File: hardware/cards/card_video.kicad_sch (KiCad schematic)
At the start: 48 parts, among them J1 HDMI_A, J2 VGA HD15, M1 Core2350B (8MB PSRAM), U2 74LVC245A, U3 74LVC245A, U4 74LVC245A, U5 74LVC245A, U6 74LVC245A, U7 74LVC245A

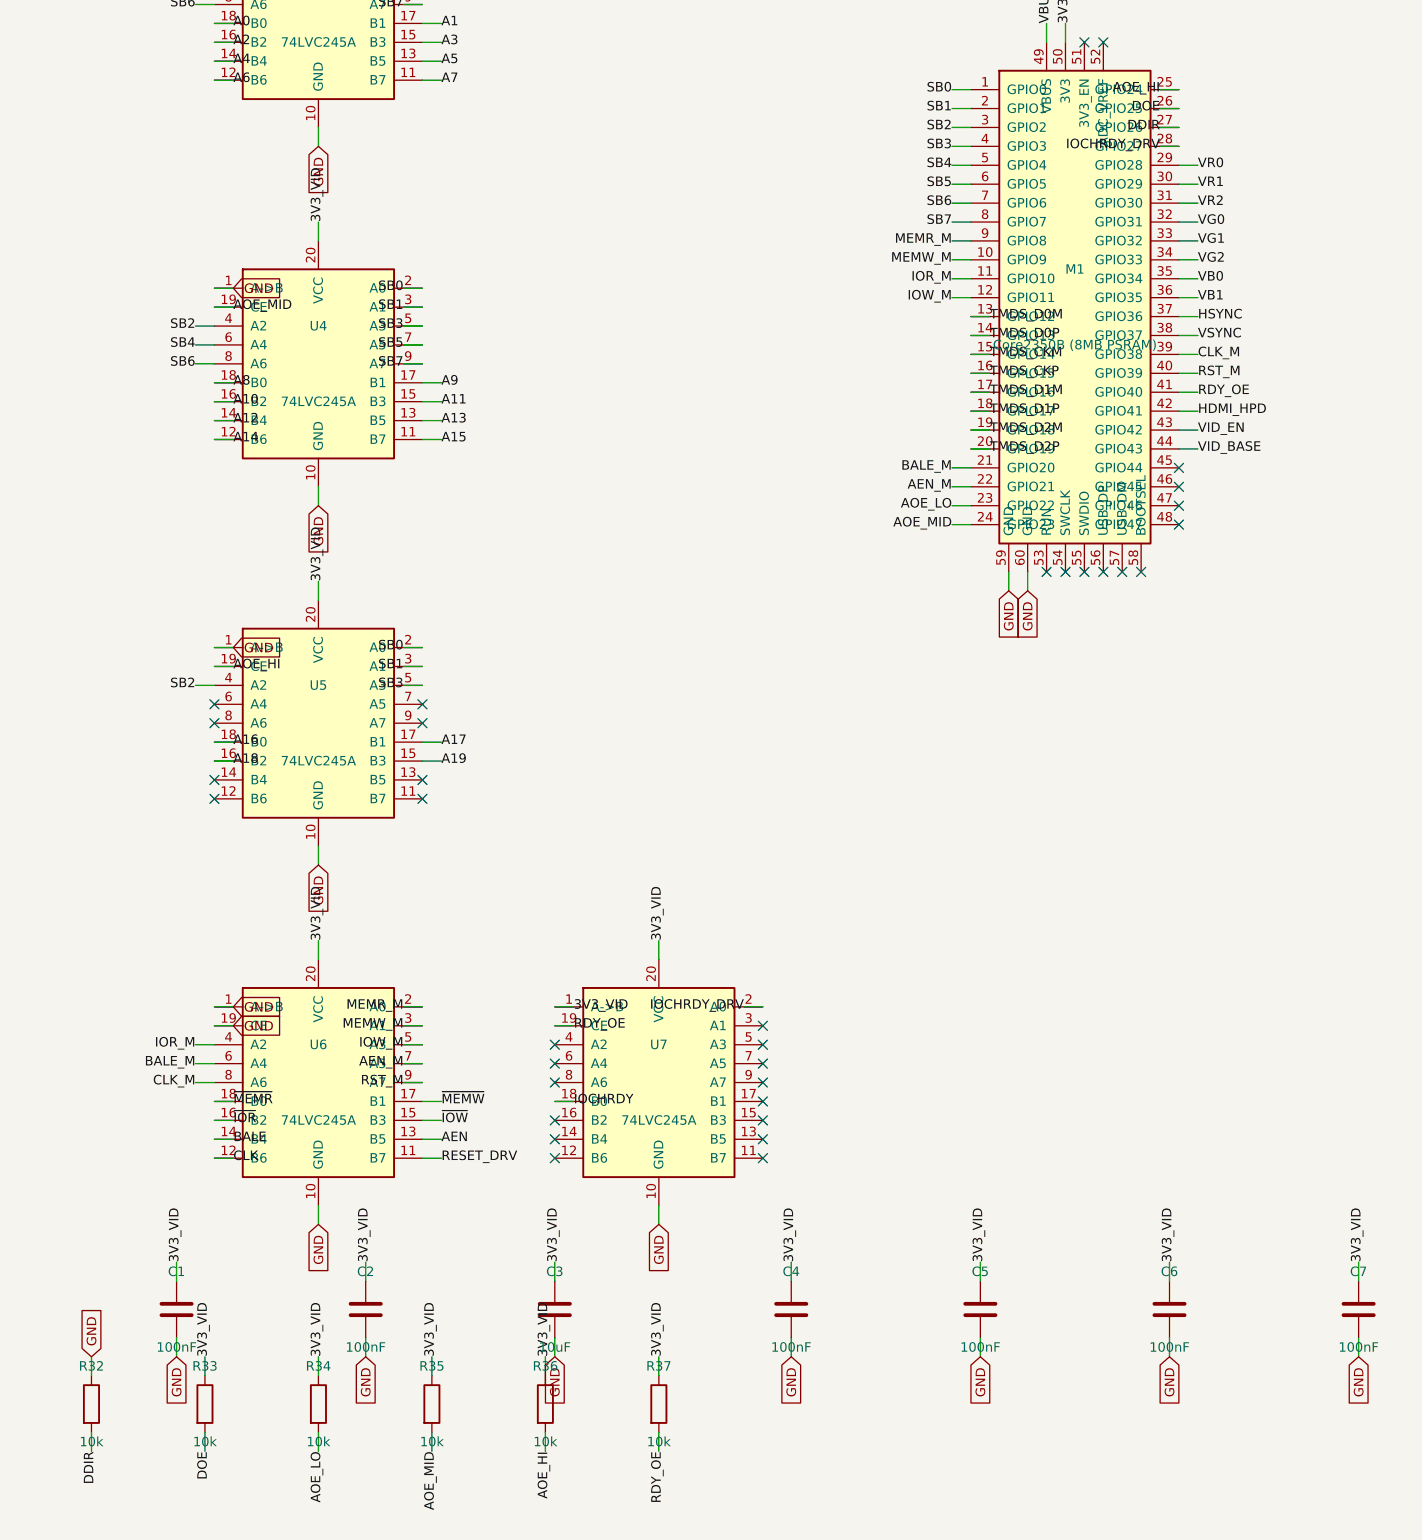
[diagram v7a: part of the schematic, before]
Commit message: sidecar: isolation/buffer bank -- 5V-compatible ISA expansion port
Rewrite the sidecar from a passive 60-pin pass-through into the 3.3V board's
only real-ISA attachment point: an LVC buffer bank (5V-tolerant inputs,
3.3V-TTL outputs) between the internal bus and an external ISA header whose
bus-side nets are port-local (X_*, via isa_conn remap).

- Outbound: 3x 74LVC245A (A0-19 + BALE/AEN/CLK/OSC, DIR strapped outbound) +
  2x 74LVC244A (MEMR/MEMW/IOR/IOW, RESET_DRV, TC, DACK1-3, REFRESH).
- Data: 1x 74LVC245A, DIR = EXP_DDIR, R1 pulls it outbound-safe at power-on
  (DIR=H => A->B; truth table in comment). ~OE tied enabled.
- Inbound: X_IRQ2-7/X_DRQ1-3 -> EXT_* via 2x 74LVC244A, 100k pull-downs on
  every X_ input (unplugged reads all-zeros).
- IOCHRDY/~{IOCHCK}: 74LVC2G07 open-drain (2G06 body + value override) drives
  the internal nets, 10k pull-ups on the X_ side (wired-AND, no contention).
- PINS: filtered copy of isa_conn.ISA_PINS (IRQ/DRQ dropped -> EXT_*), plus
  PRIV_EXP (EXP_DDIR in, EXT_* out); IOCHRDY/~{IOCHCK} kept.

Also refreshes stale build outputs from earlier 3v3 tasks that had edited
sources without rebuilding (network/picogus sheets, card_video net renames),
so committed outputs match current sources. validate_sheet sidecar: zero
structural; build.py exit 0.

Co-Authored-By: Claude Fable 5 <noreply@anthropic.com>
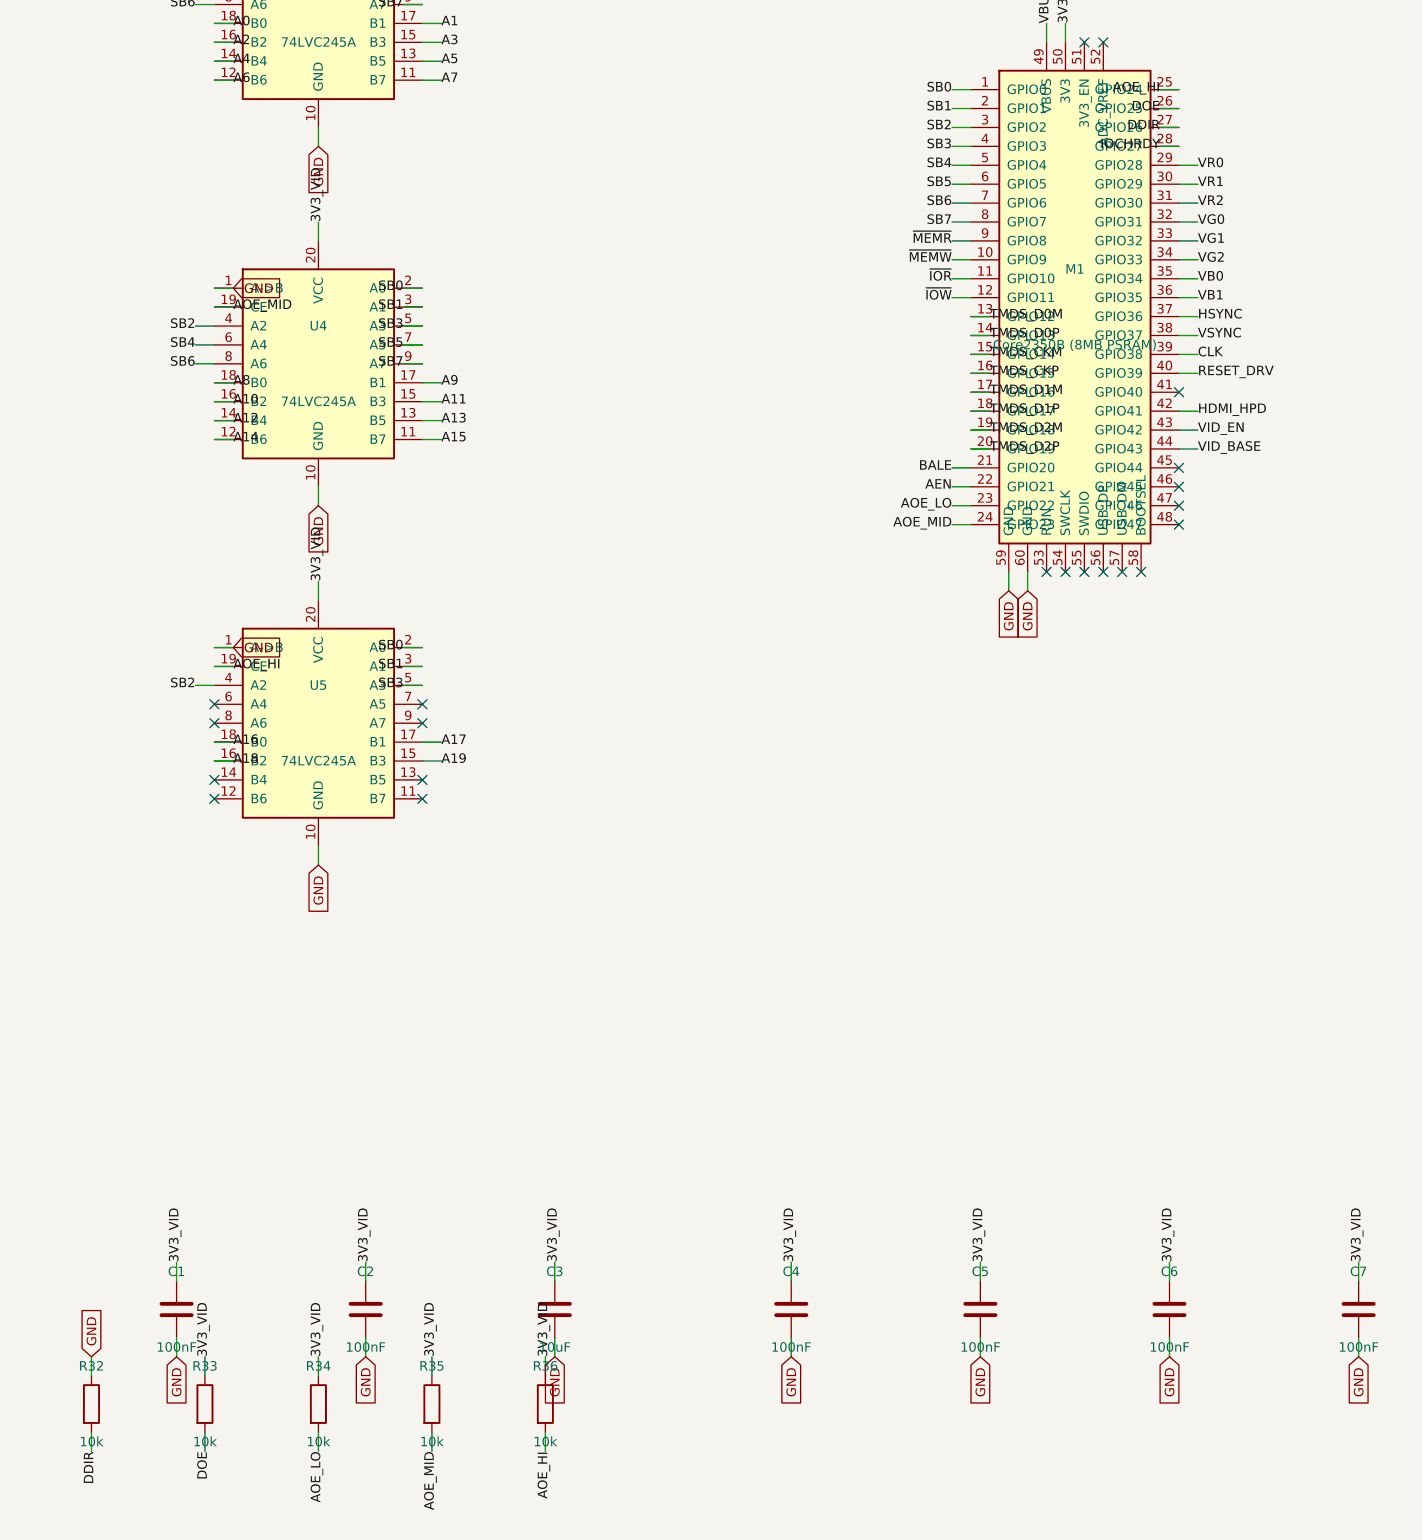
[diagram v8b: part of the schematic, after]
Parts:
- removed R10: 270, Resistor_SMD:R_0603_1608Metric, symbol Device:R
- removed R21: 1k, Resistor_SMD:R_0603_1608Metric, symbol Device:R
- removed R28: 100, Resistor_SMD:R_0603_1608Metric, symbol Device:R
- removed R37: 10k, Resistor_SMD:R_0603_1608Metric, symbol Device:R
- removed U7: 74LVC245A, Package_SO:TSSOP-20_4.4x6.5mm_P0.65mm, symbol mini-xt:74LVC245A
- added R11, R16: 270, Resistor_SMD:R_0603_1608Metric, symbol Device:R
- R10: renamed from U6; value 74LVC245A -> 270; footprint Package_SO:TSSOP-20_4.4x6.5mm_P0.65mm -> Resistor_SMD:R_0603_1608Metric; symbol mini-xt:74LVC245A -> Device:R; LCSC Part Num C6082 -> C22966
- R21: renamed from R11; value 270 -> 1k; LCSC Part Num C22966 -> C21190
- R28: renamed from R16; value 270 -> 100; LCSC Part Num C22966 -> C22775
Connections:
- net IOCHRDY_DRV is gone; now on net IOCHRDY: M1.28 (GPIO27)
- net 3V3_VID: no longer R10.20 (VCC)
- net AEN: now also M1.22 (GPIO21); no longer R10.13 (B5)
- net BALE: now also M1.21 (GPIO20); no longer R10.14 (B4)
- net CLK: now also M1.39 (GPIO38); no longer R10.12 (B6)
- net GND: no longer R10.1 (A->B), R10.10 (GND), R10.19 (CE)
- net HDMI_CKP: now also R16.2; no longer R28.2
- net HDMI_D2M: now also R11.2; no longer R21.2
- net HDMI_D2P: now also R10.2
- net HSYNC: now also R28.1
- net HSYNC_J: now also R28.2
- net RESET_DRV: now also M1.40 (GPIO39); no longer R10.11 (B7)
- net TMDS_CKP: now also R16.1; no longer R28.1
- net TMDS_D2M: now also R11.1; no longer R21.1
- net TMDS_D2P: now also R10.1
- net VGA_R: now also R21.2
- net VR1: now also R21.1
- net ~{IOR}: now also M1.11 (GPIO10); no longer R10.16 (B2)
- net ~{IOW}: now also M1.12 (GPIO11); no longer R10.15 (B3)
- net ~{MEMR}: now also M1.9 (GPIO8); no longer R10.18 (B0)
- net ~{MEMW}: now also M1.10 (GPIO9); no longer R10.17 (B1)
- removed net AEN_M: M1.22 (GPIO21), R10.7 (A5)
- removed net BALE_M: M1.21 (GPIO20), R10.6 (A4)
- removed net CLK_M: M1.39 (GPIO38), R10.8 (A6)
- removed net IOR_M: M1.11 (GPIO10), R10.4 (A2)
- removed net IOW_M: M1.12 (GPIO11), R10.5 (A3)
- removed net MEMR_M: M1.9 (GPIO8), R10.2 (A0)
- removed net MEMW_M: M1.10 (GPIO9), R10.3 (A1)
- net RDY_OE: no longer names the net of M1.41 (GPIO40)
- removed net RST_M: M1.40 (GPIO39), R10.9 (A7)
- no-connect marks 45 -> 32
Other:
- moved on the sheet: R21, R28
